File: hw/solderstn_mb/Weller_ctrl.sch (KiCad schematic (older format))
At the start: 6 parts, among them U1401 TMUX1219, U1402 TMUX1219

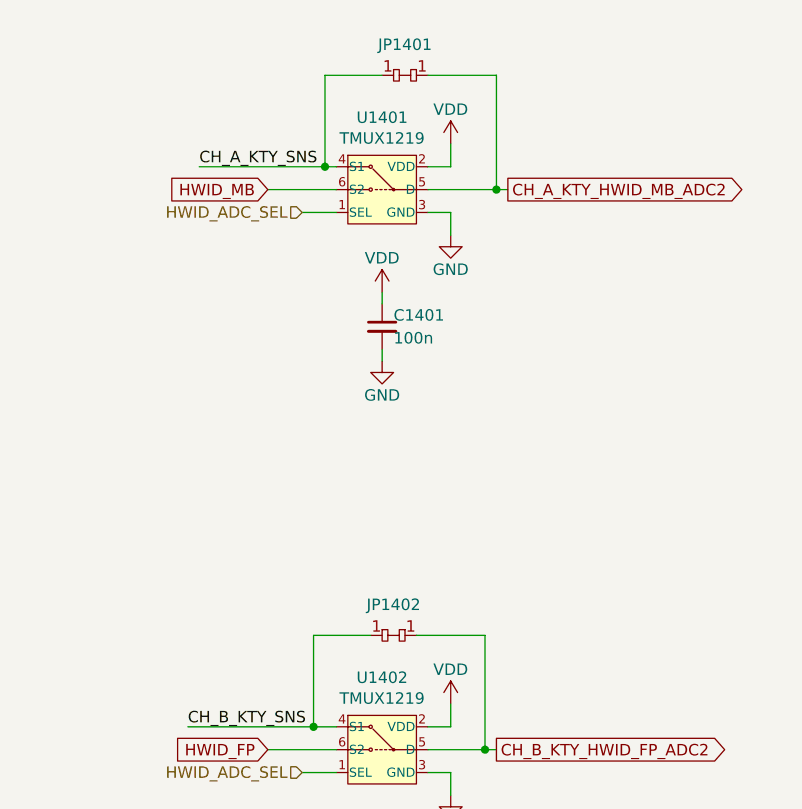
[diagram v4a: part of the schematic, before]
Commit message: Corrected several ERC issues. Re-annotated & assigned all footprints except 32k xtal (will prob. replace with RTC module anyway)
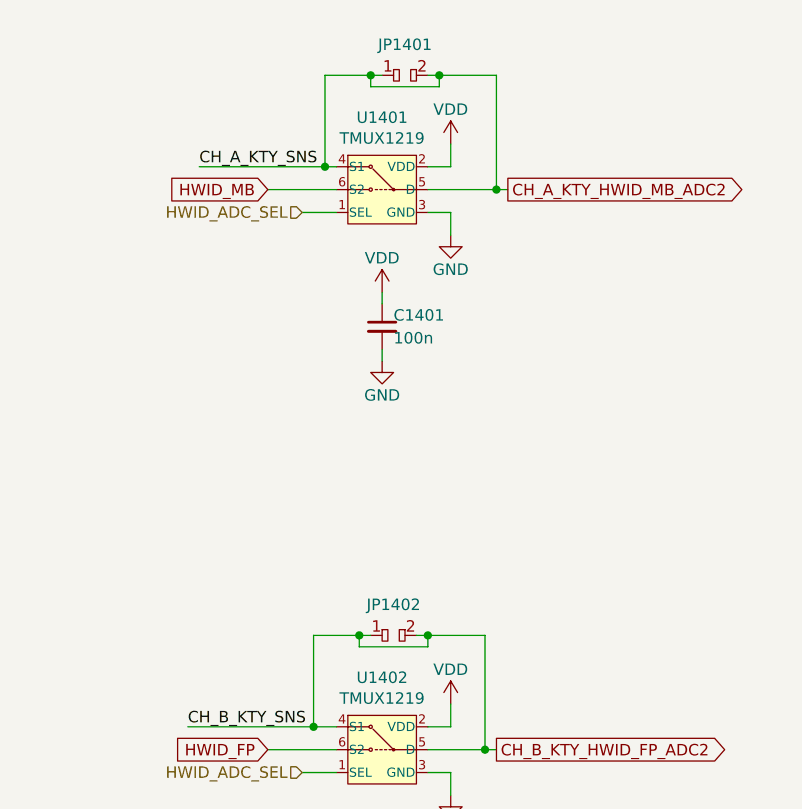
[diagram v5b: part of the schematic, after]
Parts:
- removed JP1401, JP1402: dogbone_2, customlib_mj_fp:db2_0402, symbol customlib_mj:dogbone_2
- added JP1401, JP1402: dogbone_2_ud, customlib_mj_fp:db2_ud_0402, symbol customlib_mj:dogbone_2_ud
- C1401, C1402: footprint (none) -> Capacitor_SMD:C_0603_1608Metric
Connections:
- net CH_A_KTY_SNS is gone; now on net CH_A_KTY_HWID_MB_ADC2: U1401.4 (S1)
- net CH_B_KTY_SNS is gone; now on net CH_B_KTY_HWID_FP_ADC2: U1402.4 (S1)
- net CH_A_KTY_HWID_MB_ADC2: now also JP1401.1, JP1401.2
- net CH_B_KTY_HWID_FP_ADC2: now also JP1402.1, JP1402.2
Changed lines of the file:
@@
 F 0 "C1402" H 9350 6050 50  0000 L CNN
 F 1 "100n" H 9350 5950 50  0000 L CNN
-F 2 "" H 9300 6000 50  0001 C CNN
+F 2 "Capacitor_SMD:C_0603_1608Metric" H 9300 6000 50  0001 C CNN
 F 3 "~" H 9300 6000 50  0001 C CNN
 	1    9300 6000
@@
 F 0 "C1401" H 9350 3600 50  0000 L CNN
 F 1 "100n" H 9350 3500 50  0000 L CNN
-F 2 "" H 9300 3550 50  0001 C CNN
+F 2 "Capacitor_SMD:C_0603_1608Metric" H 9300 3550 50  0001 C CNN
 F 3 "~" H 9300 3550 50  0001 C CNN
 	1    9300 3550
@@
 Wire Wire Line
 	9300 3650 9300 3700
-$Comp
-L customlib_mj:dogbone_2 JP1401
-U 1 1 5F686AB5
-P 9400 2450
-F 0 "JP1401" H 9400 2584 50  0000 C CNN
-F 1 "dogbone_2" H 9400 2550 50  0001 C CNN
-F 2 "customlib_mj_fp:db2_0402" H 9400 2450 50  0001 C CNN
-F 3 "" H 9400 2450 50  0001 C CNN
-	1    9400 2450
-	1    0    0    -1
-$EndComp
 Wire Wire Line
 	9050 2850 9050 2450
 Wire Wire Line
-	9050 2450 9300 2450
+	9050 2450 9250 2450
 Connection ~ 9050 2850
 Wire Wire Line
 	9050 2850 8500 2850
 Wire Wire Line
-	9500 2450 9800 2450
+	9500 2450 9550 2450
 Wire Wire Line
 	9800 2450 9800 2950
@@
 Wire Wire Line
 	9800 2950 9500 2950
-$Comp
-L customlib_mj:dogbone_2 JP1402
-U 1 1 5F692262
-P 9350 4900
-F 0 "JP1402" H 9350 5034 50  0000 C CNN
-F 1 "dogbone_2" H 9350 5000 50  0001 C CNN
-F 2 "customlib_mj_fp:db2_0402" H 9350 4900 50  0001 C CNN
-F 3 "" H 9350 4900 50  0001 C CNN
-	1    9350 4900
-	1    0    0    -1
-$EndComp
 Wire Wire Line
 	9000 5300 9000 4900
 Wire Wire Line
-	9000 4900 9250 4900
+	9000 4900 9200 4900
 Wire Wire Line
-	9450 4900 9750 4900
+	9450 4900 9500 4900
 Wire Wire Line
 	9750 4900 9750 5400
@@
 Wire Wire Line
 	3900 4850 3900 4800
+$Comp
+L customlib_mj:dogbone_2_ud JP1401
+U 1 1 5F4C0E49
+P 9400 2450
+F 0 "JP1401" H 9400 2584 50  0000 C CNN
+F 1 "dogbone_2_ud" H 9400 2550 50  0001 C CNN
+F 2 "customlib_mj_fp:db2_ud_0402" H 9400 2450 50  0001 C CNN
+F 3 "" H 9400 2450 50  0001 C CNN
+	1    9400 2450
+	1    0    0    -1
+$EndComp
+Wire Wire Line
+	9250 2450 9250 2500
+Wire Wire Line
+	9250 2500 9550 2500
+Wire Wire Line
+	9550 2500 9550 2450
+Connection ~ 9250 2450
+Wire Wire Line
+	9250 2450 9300 2450
+Connection ~ 9550 2450
+Wire Wire Line
+	9550 2450 9800 2450
+$Comp
+L customlib_mj:dogbone_2_ud JP1402
+U 1 1 5F4C3BF6
+P 9350 4900
+F 0 "JP1402" H 9350 5034 50  0000 C CNN
+F 1 "dogbone_2_ud" H 9350 5000 50  0001 C CNN
+F 2 "customlib_mj_fp:db2_ud_0402" H 9350 4900 50  0001 C CNN
+F 3 "" H 9350 4900 50  0001 C CNN
+	1    9350 4900
+	1    0    0    -1
+$EndComp
+Wire Wire Line
+	9200 4900 9200 4950
+Wire Wire Line
+	9200 4950 9500 4950
+Wire Wire Line
+	9500 4950 9500 4900
+Connection ~ 9200 4900
+Wire Wire Line
+	9200 4900 9250 4900
+Connection ~ 9500 4900
+Wire Wire Line
+	9500 4900 9750 4900
 $EndSCHEMATC
